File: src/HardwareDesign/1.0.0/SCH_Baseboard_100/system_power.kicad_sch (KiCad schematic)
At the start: 0 parts

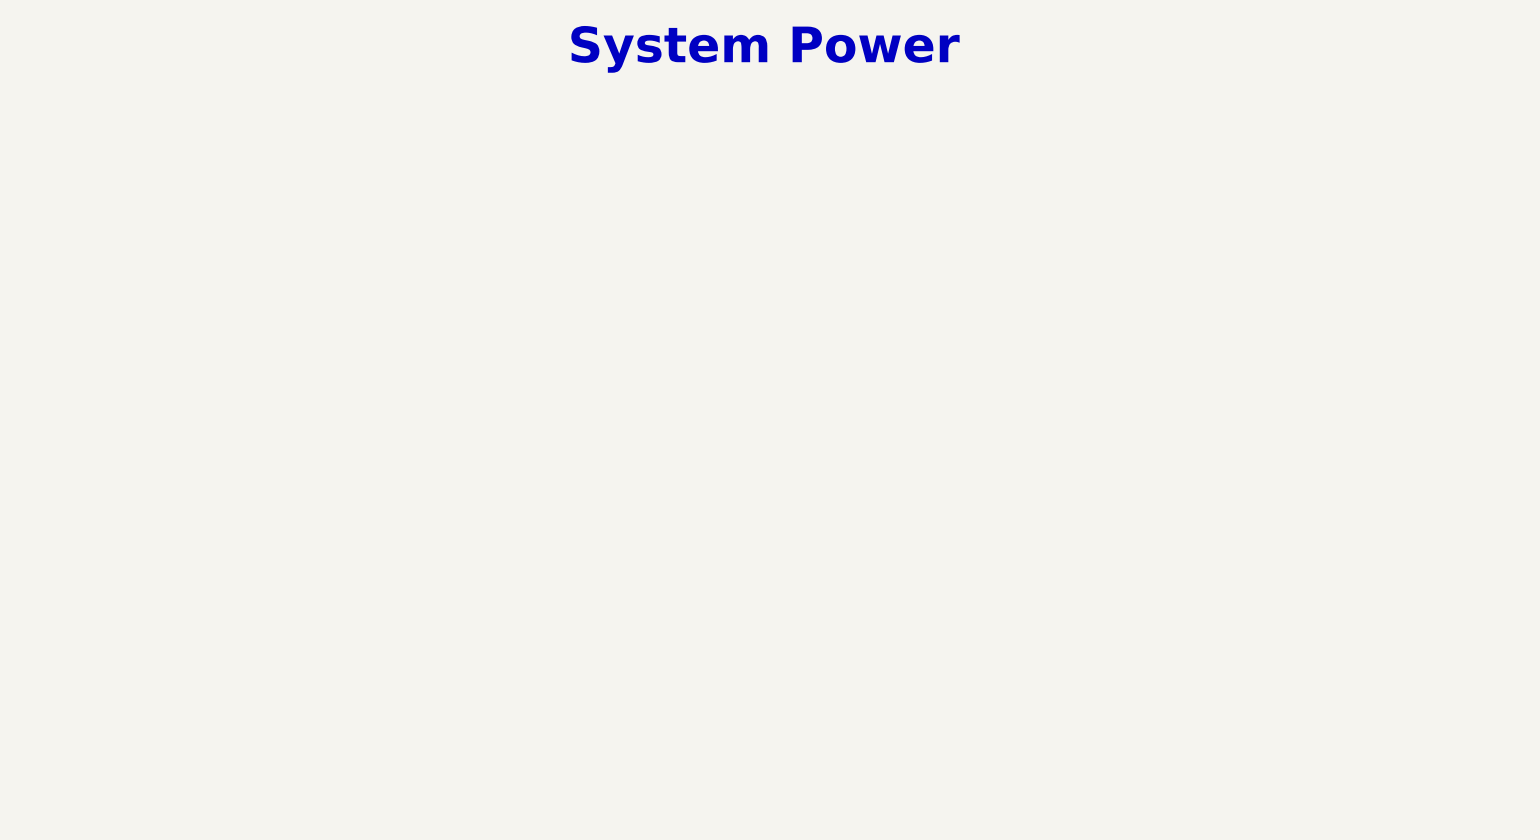
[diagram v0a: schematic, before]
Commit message: Add bladecore to design
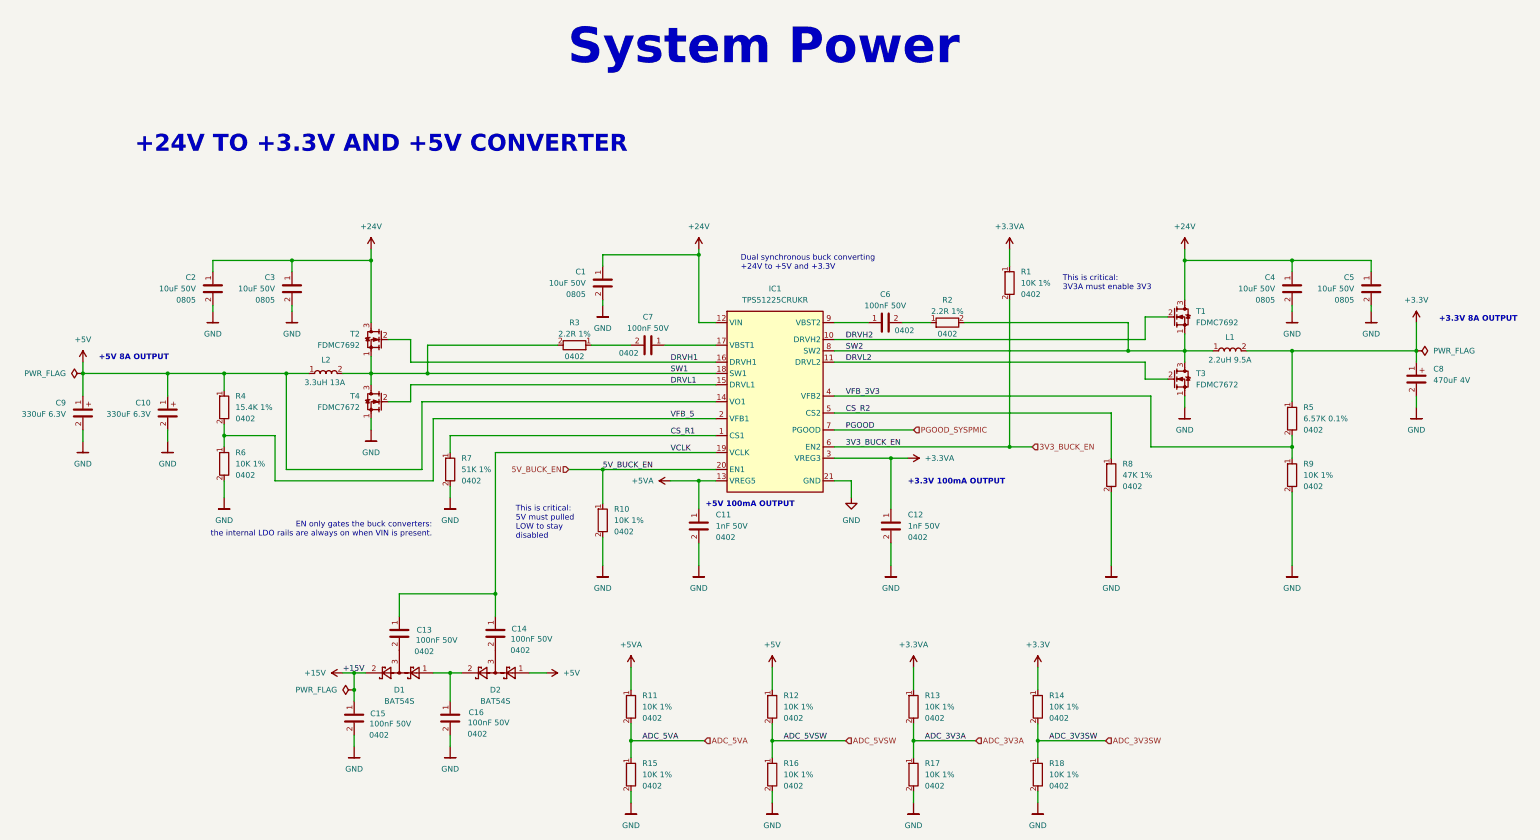
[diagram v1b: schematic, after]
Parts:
- added C1, C2, C3, C4, C5: 10uF 50V, Capacitor_SMD:C_0805_2012Metric, symbol DS_Capacitor_0805:10uF 50V 0805
- added C10, C9: 330uF 6.3V, DS_Capacitor:2917, symbol DS_Capacitor_Tantal:330uF_6.3V
- added C11, C12: 1nF 50V, Capacitor_SMD:C_0402_1005Metric, symbol DS_Capacitor_0402:1nF 50V 0402
- added C13, C14, C15, C16, C6, C7: 100nF 50V, Capacitor_SMD:C_0402_1005Metric, symbol DS_Capacitor_0402:100nF 50V 0402
- added C8: 470uF 4V, DS_Capacitor:2917, symbol DS_Capacitor_Tantal:470uF_4V
- added D1, D2: BAT54S, DS_Diode:SOT23-3, symbol DS_Diode:BAT54S
- added IC1: TPS51225CRUKR, DS_Vreg:QFN20-3x3, symbol DS_Vreg:TPS51225C
- added L1: 2.2uH 9.5A, DS_Inductor:7x6.6mm, symbol DS_Inductor:2.2uH_9.5A
- added L2: 3.3uH 13A, DS_Inductor:7x6.6mm, symbol DS_Inductor:3.3uH 13A
- added R1, R10, R11, R12, R13, R14, R15, R16, R17, R18, R6, R9: 10K 1%, Resistor_SMD:R_0402_1005Metric, symbol DS_Resistor_0402:10K 1% 0402
- added R2, R3: 2.2R 1%, Resistor_SMD:R_0402_1005Metric, symbol DS_Resistor_0402:2.2R 1% 0402
- added R4: 15.4K 1%, Resistor_SMD:R_0402_1005Metric, symbol DS_Resistor_0402:15.4K 1% 0402
- added R5: 6.57K 0.1%, Resistor_SMD:R_0402_1005Metric, symbol DS_Resistor_0402:6.57K_1%
- added R7: 51K 1%, Resistor_SMD:R_0402_1005Metric, symbol DS_Resistor_0402:51K_1%
- added R8: 47K 1%, Resistor_SMD:R_0402_1005Metric, symbol DS_Resistor_0402:47K_1%
- added T1, T2: FDMC7692, DS_FET:DFN8_3x3, symbol DS_FET:FDMC7692
- added T3, T4: FDMC7672, DS_FET:DFN8_3x3, symbol DS_FET:FDMC7672
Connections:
- new net: C7.1, IC1.17 (VBST1)
- new net: C6.1, IC1.9 (VBST2)
- new net: C13.2, D1.3
- new net: C6.2, R2.1
- new net: C14.2, D2.3
- new net: C16.1, D1.1, D2.2
- new net: C7.2, R3.1
- new net +15V: C15.1, D1.2
- new net +24V: C1.1, C2.1, C3.1, C4.1, C5.1, IC1.12 (VIN), T1.3, T2.3
- new net +3.3V: C8.1, L1.2, R14.1, R5.1
- new net +3.3VA: C12.1, IC1.3 (VREG3), R1.1, R13.1
- new net +5V: C10.1, C9.1, D2.1, IC1.14 (VO1), L2.1, R12.1, R4.1
- new net +5VA: C11.1, IC1.13 (VREG5), R11.1
- new net 3V3_BUCK_EN: IC1.6 (EN2), R1.2
- new net 5V_BUCK_EN: IC1.20 (EN1), R10.1
- new net ADC_3V3A: R13.2, R17.1
- new net ADC_3V3SW: R14.2, R18.1
- new net ADC_5VA: R11.2, R15.1
- new net ADC_5VSW: R12.2, R16.1
- new net CS_R1: IC1.1 (CS1), R7.1
- new net CS_R2: IC1.5 (CS2), R8.1
- new net DRVH1: IC1.16 (DRVH1), T2.2
- new net DRVH2: IC1.10 (DRVH2), T1.2
- new net DRVL1: IC1.15 (DRVL1), T4.2
- new net DRVL2: IC1.11 (DRVL2), T3.2
- new net GND: C1.2, C10.2, C11.2, C12.2, C15.2, C16.2, C2.2, C3.2, C4.2, C5.2, C8.2, C9.2, IC1.21 (GND), R10.2, R15.2, R16.2, R17.2, R18.2, R6.2, R7.2, R8.2, R9.2, T3.1, T4.1
- new net PGOOD_SYSPMIC: IC1.7 (PGOOD)
- new net SW1: IC1.18 (SW1), L2.2, R3.2, T2.1, T4.3
- new net SW2: IC1.8 (SW2), L1.1, R2.2, T1.1, T3.3
- new net VCLK: C13.1, C14.1, IC1.19 (VCLK)
- new net VFB_3V3: IC1.4 (VFB2), R5.2, R9.1
- new net VFB_5: IC1.2 (VFB1), R4.2, R6.1
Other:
- note added: "+24V TO +3.3V AND +5V CONVERTER"
- note added: "+3.3V 100mA OUTPUT"
- note added: "+3.3V 8A OUTPUT"
- note added: "+5V 100mA OUTPUT"
- note added: "+5V 8A OUTPUT"
- note added: "Dual synchronous buck converting +24V to +5V and +3.3V"
- note added: "EN only gates the buck converters: the internal LDO rails are always on when VIN is present."
- note added: "This is critical: 3V3A must enable 3V3"
- note added: "This is critical: 5V must pulled LOW to stay disabled"
